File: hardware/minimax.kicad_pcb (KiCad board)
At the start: 4 copper layers, 35 x 40 mm, 60 parts, among them J1 524352271, J2 59S1AC-40MT5-Z, J3 PRT-14417, J4 PRT-14417, Q1 DMG1012T, Q2 DMG1012T, Q3 DMG1012T, U1 MAX96717GTJ/VY+, U2 MAX20049ATED/VY+

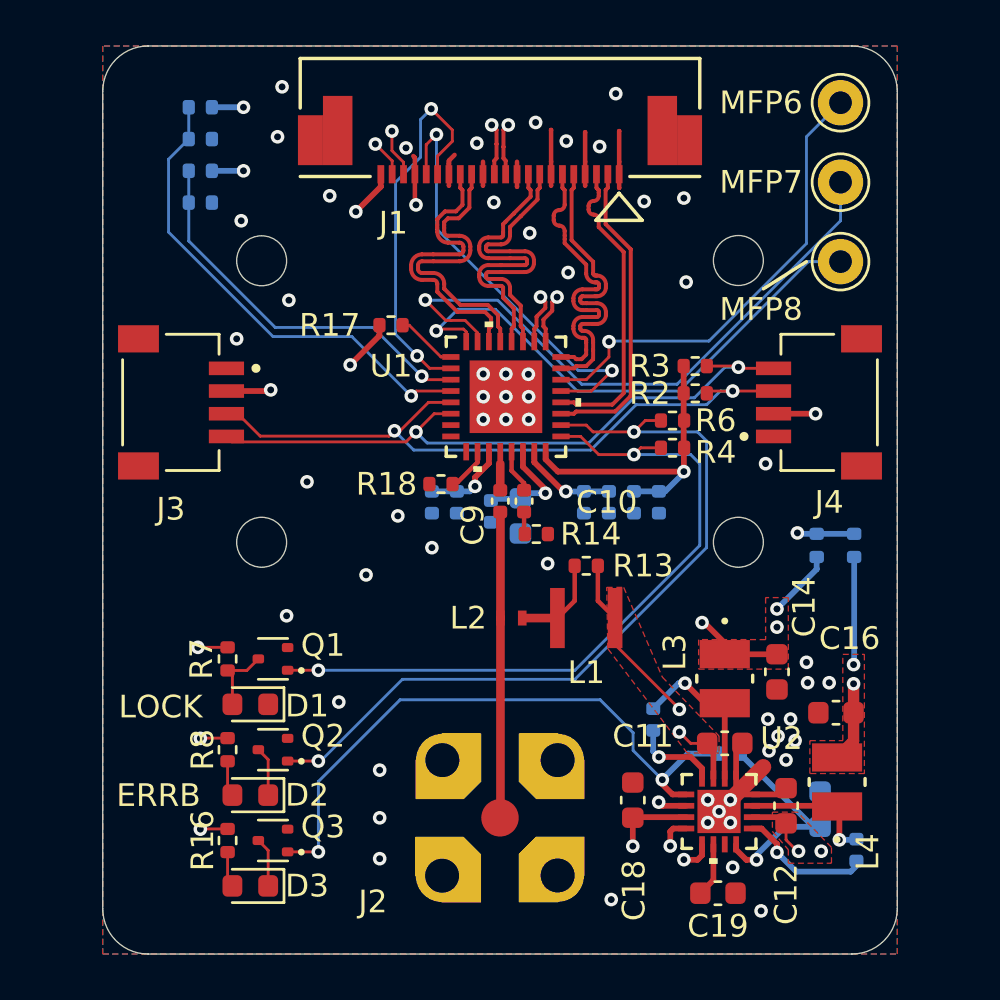
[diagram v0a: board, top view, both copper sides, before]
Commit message: fixed LED logic and added pullup on the camera enable
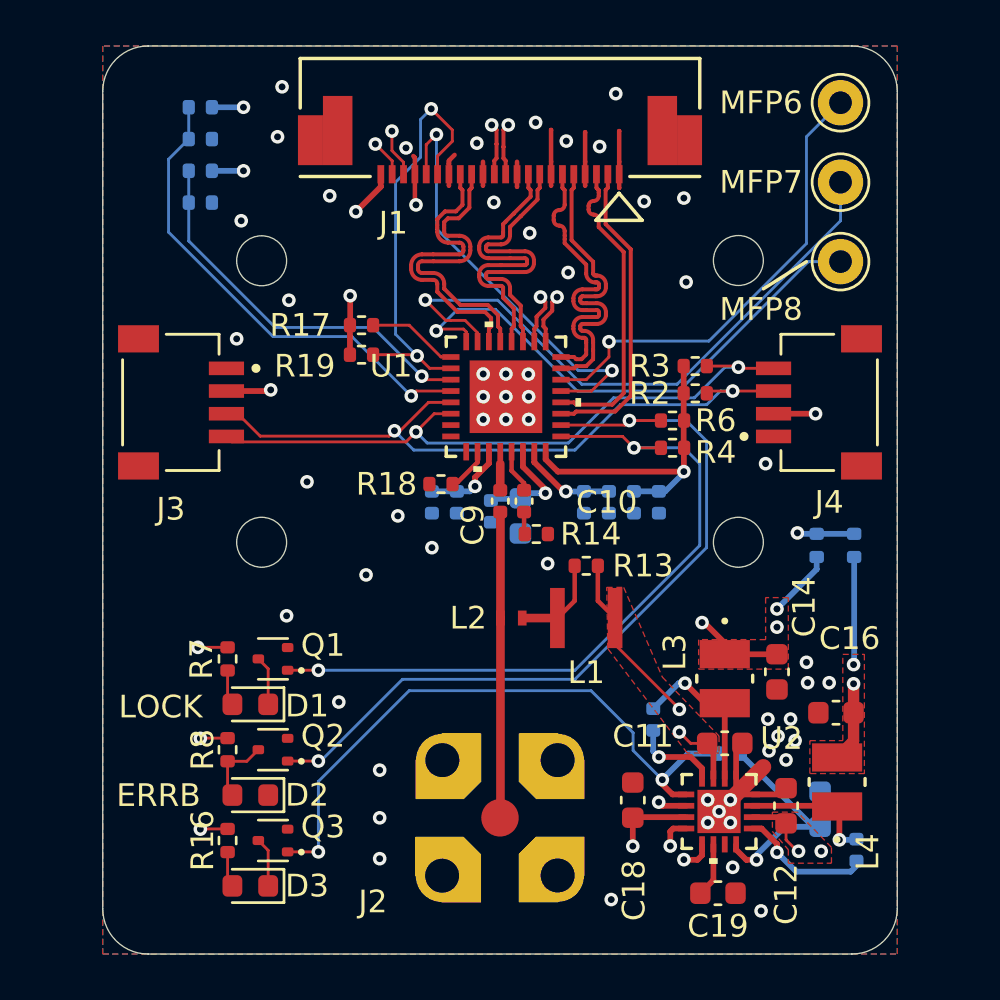
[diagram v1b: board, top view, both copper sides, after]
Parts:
- added R19: 5.1K, Resistor_SMD:R_0402_1005Metric, F.Cu at (143.9, 101.6)
- moved R17 1.30 mm to (143.9, 100.3)
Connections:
- D1 pad 1: GND -> Net-(D1-K)
- D2 pad 1: Net-(D2-K) -> GND
- Q1 pad 3: Net-(D1-A) -> Net-(D1-K)
- Q2 pad 3: Net-(D2-K) -> Net-(D2-A)
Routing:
- net Net-(D2-K): track 2.18 -> 0.00 mm
- net Net-(D1-K): track 0.00 -> 2.18 mm
- net /camera/POWER_EN: track 17.2 -> 19.1 mm
- net Net-(D1-A): track 3.14 -> 1.58 mm
- net Net-(D2-A): track 1.58 -> 3.14 mm
- net Net-(U1-PWDNB): track 2.71 -> 4.01 mm

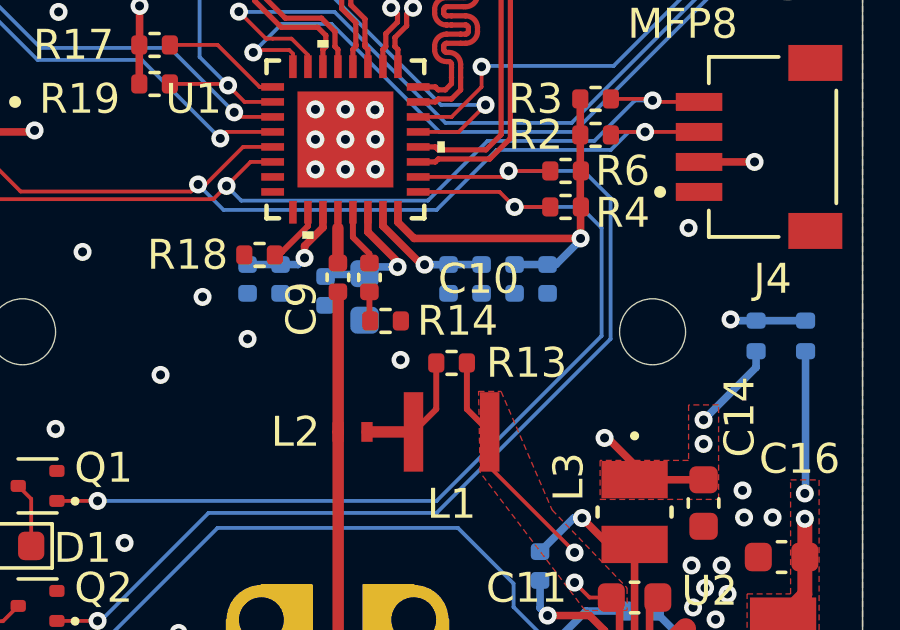
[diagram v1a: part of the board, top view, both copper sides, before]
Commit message: minor layout optimizations
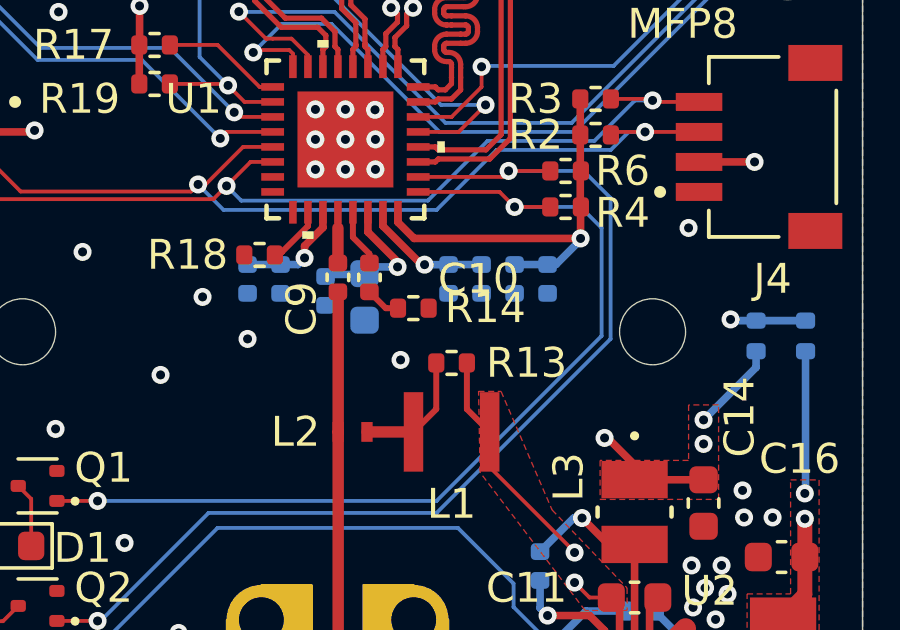
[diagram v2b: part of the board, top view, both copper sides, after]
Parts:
- moved R14 1.02 mm to (152.5, 109.1)
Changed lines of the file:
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@@
 	(footprint "Resistor_SMD:R_0402_1005Metric"
 		(layer "F.Cu")
-		(at 151.6 109.5)
+		(at 152.525 109.075)
 		(descr "Resistor SMD 0402 (1005 Metric), square (rectangular) end terminal, IPC_7351 nominal, (Body size source: IPC-SM-782 page 72, https://www.pcb-3d.com/wordpress/wp-content/uploads/ipc-sm-782a_amendment_1_and_2.pdf), generated with kicad-footprint-generator")
 		(tags "resistor")
@@
 			(size 2.32 2.32)
 			(drill 1.5)
-			(layers "*.Cu" "*.Mask")
+			(layers "*.Cu" "*.Paste" "*.Mask")
 			(remove_unused_layers no)
 			(net 20 "GND")
@@
 			(size 2.32 2.32)
 			(drill 1.5)
-			(layers "*.Cu" "*.Mask")
+			(layers "*.Cu" "*.Paste" "*.Mask")
 			(remove_unused_layers no)
 			(net 20 "GND")
@@
 			(size 2.32 2.32)
 			(drill 1.5)
-			(layers "*.Cu" "*.Mask")
+			(layers "*.Cu" "*.Paste" "*.Mask")
 			(remove_unused_layers no)
 			(net 20 "GND")
@@
 			(size 2.32 2.32)
 			(drill 1.5)
-			(layers "*.Cu" "*.Mask")
+			(layers "*.Cu" "*.Paste" "*.Mask")
 			(remove_unused_layers no)
 			(net 20 "GND")
@@
 	)
 	(segment
-		(start 151.0611 108.53)
-		(end 151.0611 109.54)
+		(start 152.015 109.075)
+		(end 151.6061 109.075)
+		(width 0.2)
+		(layer "F.Cu")
+		(net 14)
+	)
+	(segment
+		(start 151.6061 109.075)
+		(end 151.0611 108.53)
+		(width 0.2)
+		(layer "F.Cu")
+		(net 14)
+	)
+	(segment
+		(start 151.0811 108.55)
+		(end 151.0611 108.53)
 		(width 0.2)
 		(layer "F.Cu")
@@
 	)
 	(zone
-		(net 5)
-		(net_name "Net-(C9-Pad2)")
-		(layer "F.Cu")
-		(name "$teardrop_padvia$")
-		(hatch full 0.1)
-		(priority 30000)
-		(attr
-			(teardrop
-				(type padvia)
-			)
-		)
-		(connect_pads yes
-			(clearance 0)
-		)
-		(min_thickness 0.0254)
-		(filled_areas_thickness no)
-		(fill yes
-			(thermal_gap 0.5)
-			(thermal_bridge_width 0.5)
-			(island_removal_mode 1)
-			(island_area_min 10)
-		)
-		(polygon
-			(pts
-				(xy 150.2105 120.353978) (xy 149.8295 120.353978) (xy 149.237799 121.684286) (xy 150 122.001) (xy 150.762201 121.684286)
-			)
-		)
-	)
-	(zone
 		(net 32)
 		(net_name "/connector/V_POC")
@@
 	)
 	(zone
+		(net 5)
+		(net_name "Net-(C9-Pad2)")
+		(layer "F.Cu")
+		(name "$teardrop_padvia$")
+		(hatch full 0.1)
+		(priority 30000)
+		(attr
+			(teardrop
+				(type padvia)
+			)
+		)
+		(connect_pads yes
+			(clearance 0)
+		)
+		(min_thickness 0.0254)
+		(filled_areas_thickness no)
+		(fill yes
+			(thermal_gap 0.5)
+			(thermal_bridge_width 0.5)
+			(island_removal_mode 1)
+			(island_area_min 10)
+		)
+		(polygon
+			(pts
+				(xy 150.2105 120.353978) (xy 149.8295 120.353978) (xy 149.237799 121.684286) (xy 150 122.001) (xy 150.762201 121.684286)
+			)
+		)
+	)
+	(zone
 		(net 0)
 		(net_name "")
@@
 		(polygon
 			(pts
+				(xy 150.375 106.26) (xy 150.375 105.49) (xy 150.635 105.49) (xy 150.635 106.26)
+			)
+		)
+	)
+	(zone
+		(net 0)
+		(net_name "")
+		(layer "In1.Cu")
+		(hatch edge 0.5)
+		(connect_pads
+			(clearance 0)
+		)
+		(min_thickness 0.25)
+		(filled_areas_thickness no)
+		(keepout
+			(tracks not_allowed)
+			(vias not_allowed)
+			(pads not_allowed)
+			(copperpour not_allowed)
+			(footprints allowed)
+		)
+		(fill
+			(thermal_gap 0.5)
+			(thermal_bridge_width 0.5)
+		)
+		(polygon
+			(pts
 				(xy 149.83 112.87) (xy 151.17 112.87) (xy 151.17 113.53) (xy 149.83 113.53)
 			)
 		)
+	)
+	(zone
+		(net 0)
+		(net_name "")
+		(layer "In1.Cu")
+		(hatch edge 0.5)
+		(connect_pads
+			(clearance 0)
+		)
+		(min_thickness 0.25)
+		(filled_areas_thickness no)
+		(keepout
+			(tracks not_allowed)
+			(vias not_allowed)
+			(pads not_allowed)
+			(copperpour not_allowed)
+			(footprints allowed)
+		)
+		(fill
+			(thermal_gap 0.5)
+			(thermal_bridge_width 0.5)
+		)
+		(polygon
+			(pts
+				(xy 150.755 108.81) (xy 150.755 107.29) (xy 151.375 107.29) (xy 151.375 108.81)
+			)
+		)

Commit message: prepping for fab
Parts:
- removed H1, H2, H3, H4: MountingHole, MountingHole:MountingHole_2.2mm_M2
- removed MFP6, MFP7, MFP8: TestPoint, Connector_Pin:Pin_D1.0mm_L10.0mm
- added J5: RPI-CAM-V2_1, user:RPI-CAM-V2_1, F.Cu at (150.2, 88.0)
- added TP1: MFP8, TestPoint:TestPoint_THTPad_D1.0mm_Drill0.5mm, F.Cu at (132.0, 126.0)
- added TP2: MFP7, TestPoint:TestPoint_THTPad_D1.0mm_Drill0.5mm, F.Cu at (132.0, 123.5)
- added TP3: MFP6, TestPoint:TestPoint_THTPad_D1.0mm_Drill0.5mm, F.Cu at (132.0, 121.0)
- C1, C13, C15, C17, C2, C3, C4, C5, C6, C7, C8, R1, R10, R11, R12, R15, R5: moved to F.Cu
- R9: value 5.1K -> 5.1k; moved to F.Cu
- moved R9 41.6 mm to (164.0, 125.0)
- moved R11 41.5 mm to (164.0, 126.2)
- moved R10 41.3 mm to (164.0, 121.8)
- moved R12 41.2 mm to (164.0, 123.0)
- moved D3 37.5 mm to (161.5, 95.0), turned to 0 degrees
- moved R16 35.7 mm to (162.5, 97.0), turned to 90 degrees
- moved J1 33.7 mm to (150.0, 124.8), turned to 0 degrees
- moved J4 33.6 mm to (132.8, 115.0), turned to -90 degrees
- moved Q3 33.1 mm to (160.7, 97.2), turned to 90 degrees
- moved J2 28.0 mm to (150.0, 94.0), turned to 180 degrees
- moved D2 26.0 mm to (140.6, 95.0), turned to 0 degrees
- moved D1 22.5 mm to (134.2, 95.0), turned to 0 degrees
- moved R8 22.3 mm to (141.6, 97.0), turned to 90 degrees
- moved Q2 21.8 mm to (139.9, 97.2), turned to 90 degrees
- moved R3 21.8 mm to (140.8, 114.6), turned to 180 degrees
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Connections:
- L4 pad 1: Net-(U2-LX1) -> +3V3
- L4 pad 2: +3V3 -> Net-(U2-LX1)
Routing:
- net Net-(U1-MFP8): track 23.9 -> 40.0 mm
- net VDDIO: track 59.6 -> 75.5 mm
- net /gmsl/ERRB: track 35.3 -> 21.7 mm
- net Net-(U1-MFP7): track 27.8 -> 40.0 mm
- net /gmsl/LOCK: track 32.1 -> 22.7 mm
- net Net-(Q3-G): track 27.7 -> 37.1 mm, vias 2 -> 3
- net +1V8: track 41.9 -> 34.6 mm, vias 5 -> 4
- net +1V2: track 24.9 -> 30.9 mm
- net +3V3: track 22.4 -> 28.2 mm, vias 10 -> 11
- net Net-(U2-BIAS): track 9.69 -> 4.35 mm, vias 1 -> 0
- net /camera/POWER_EN: track 19.1 -> 14.6 mm
- net /camera/MFP9_SDA: track 44.8 -> 48.7 mm, vias 3 -> 4
- net MFP1_CFG0: track 17.3 -> 21.0 mm, vias 1 -> 2
- net /camera/LED_EN: track 19.0 -> 15.4 mm
- net MFP2_CFG1: track 21.4 -> 18.8 mm, vias 1 -> 2
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- added copper zone on B.Cu, net /connector/V_POC
- removed copper zone on In2.Cu, net +1V2
- removed copper zone on In2.Cu, net +1V8
- removed copper zone on In2.Cu, net VDDIO
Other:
- board size 35 x 40 mm -> 40 x 40 mm
- rule pad_to_mask_clearance: 0.0762 -> 0.05
- board text added: "1V8"
- board text added: "3V3"
- board text added: "Layer Material Thickness L1 Outer Copper, 1oz 0.035 Prepreg 7628, RC 49%, 8.6 mil 0.2104 L2 Inner Copper, 0.5oz 0.0152 Core 1.1mm H/HOZ with copper 1.065 L3 Inner Copper, 0.5oz 0.0152 Prepreg 7628, RC 49%, 8.6 mil 0.2104 L4 Outer Copper, 1oz 0.035"
- board text added: "Layer Name Function 1 F.Cu Signal 2 In1.Cu GND (Controlled Impedance) 3 In1.Cu Power 4 B.Cu GND JLC Stackup JLC04161H-7628(Standard/Finished thickness1.59mm±10%) 100Ohm Diff-pair: W=0.155 S=0.13 50Ohm Single Ended: W=0.35"
- board text added: "MFP6"
- board text added: "MFP7"
- board text added: "MFP8"
- board text added: "PGOOD"
- board text added: "VDDIO"
- board text removed: "Layer Name Function 1 F.Cu Signal 2 In1.Cu GND (Controlled Impedance) 3 In1.Cu Power 4 B.Cu GND"
- board text removed: "VDDIO 1V8- 3V3-"
